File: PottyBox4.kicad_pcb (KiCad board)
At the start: 2 copper layers, 46 parts, among them IC1 ESP32-WROVER-B_(16MB), J1 Sensor 1, J10 Flush 2, J2 Touch 1, J3 24VAC, J4 Sensor 2, J5 Touch 2, J6 Qwiic, J7 DEGUG, J8 Exhaust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

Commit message: Finish up schematic, start layout work
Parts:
- added D10: PWR, LED_SMD:LED_0603_1608Metric_Pad1.05x0.95mm_HandSolder, F.Cu at (176.1, 95.3)
- added D9: STATUS, ASMB-KTF0-0A306:ASMBKTF00A306, F.Cu at (118.5, 124.5)
- added R16: 1k, Resistor_SMD:R_0603_1608Metric_Pad1.05x0.95mm_HandSolder, F.Cu at (117.5, 121.0)
- added R17: 1k, Resistor_SMD:R_0603_1608Metric_Pad1.05x0.95mm_HandSolder, F.Cu at (171.6, 107.5)
- added SW1: BOOT, PTS526_SMG15_SMTR2_LFS:PTS526SMG15SMTR2LFS, F.Cu at (227.1, 125.7)
- added SW2: RESET, PTS526_SMG15_SMTR2_LFS:PTS526SMG15SMTR2LFS, F.Cu at (227.1, 117.6)
- D2: value GREEN -> S1
- D3: value GREEN -> S2
- D4: value F1 -> S1S
- D5: value F2 -> S2S
- D6: value EX -> F1
- D7: value STATUS -> F2; footprint ASMB-KTF0-0A306:ASMBKTF00A306 -> LED_SMD:LED_0603_1608Metric_Pad1.05x0.95mm_HandSolder
- D8: value PWR -> EX
- IC1: value ESP32-WROVER-B_(16MB) -> ESP32-WROVER-B
- J3: value 24VAC -> Sensor 2; footprint SparkFun-Connectors:SCREWTERMINAL-3.5MM-2 -> Connector_JST:JST_SH_SM06B-SRSS-TB_1x06-1MP_P1.00mm_Horizontal
- J4: value Sensor 2 -> Touch 2; footprint Connector_JST:JST_SH_SM06B-SRSS-TB_1x06-1MP_P1.00mm_Horizontal -> Connector_JST:JST_PH_S2B-PH-K_1x02_P2.00mm_Horizontal
- J5: value Touch 2 -> Qwiic; footprint Connector_JST:JST_PH_S2B-PH-K_1x02_P2.00mm_Horizontal -> Connector_JST:JST_SH_SM04B-SRSS-TB_1x04-1MP_P1.00mm_Horizontal
- J6: value Qwiic -> 24VAC; footprint Connector_JST:JST_SH_SM04B-SRSS-TB_1x04-1MP_P1.00mm_Horizontal -> SparkFun-Connectors:SCREWTERMINAL-3.5MM-2
- K1, K2: value G3VM-61VY3(TR05) -> G3VM-61VY3
- R1, R2, R5: value 10k -> 1k
- R11, R12: value 1k -> 220
- R3, R4, R7: value 1k -> 10k
- R8, R9: value 220 -> 1k
- U1: value RPM3.3-2.0 -> OKI-78SR-3.3/1.5-W36H-C; footprint Converter_DCDC:Converter_DCDC_RECOM_RPMx.x-x.0 -> Converter_DCDC:Converter_DCDC_muRata_OKI-78SR_Horizontal
- moved J9 211.8 mm to (34.2, 115.8)
- moved R8 211.0 mm to (33.2, 103.5), turned to 90 degrees
- moved R10 199.1 mm to (37.8, 102.5), turned to 180 degrees
- moved C1 196.3 mm to (44.8, 50.2), turned to 90 degrees
- moved R11 193.7 mm to (50.2, 102.5), turned to 180 degrees
- moved K1 192.1 mm to (37.2, 107.8), turned to -90 degrees
- moved R12 191.1 mm to (72.8, 106.8), turned to 180 degrees
- moved R9 190.3 mm to (45.8, 103.5), turned to 90 degrees
- moved J10 186.5 mm to (46.8, 115.8)
- moved K3 176.2 mm to (78.2, 118.2), turned to 90 degrees
- moved R13 173.6 mm to (69.2, 106.8)
- moved U1 173.1 mm to (44.8, 60.8)
- moved K2 173.1 mm to (49.8, 107.8), turned to -90 degrees
- moved D8 172.4 mm to (65.8, 106.8)
- moved J6 160.3 mm to (50.5, 49.0)
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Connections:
- IC1 pad 10: (no net) -> /FLUSH1
- IC1 pad 11: (no net) -> /FLUSH2
- IC1 pad 12: (no net) -> /LED_SR
- IC1 pad 13: (no net) -> /LED_SG
- IC1 pad 14: (no net) -> /LED_SB
- IC1 pad 16: (no net) -> /EXHAUST
- IC1 pad 24: (no net) -> /SHUT1
- IC1 pad 26: (no net) -> /SHUT2
- IC1 pad 29: (no net) -> /INT1
- IC1 pad 30: (no net) -> /INT2
- IC1 pad 31: (no net) -> /LED_S1
- IC1 pad 37: (no net) -> /LED_S2
- J1 pad 5: (no net) -> /INT1
- J1 pad 6: (no net) -> /SHUT1
- J3 pad 1: /24VAC1 -> GND
- J3 pad 2: /24VAC2 -> +3V3
- J4 pad 2: +3V3 -> /TOUCH2
- J5 pad 2: /TOUCH2 -> +3V3
- J6 pad 1: GND -> /24VAC1
- J6 pad 2: +3V3 -> /24VAC2
- R1 pad 1: Net-(Q1-Pad1) -> Net-(D2-Pad2)
- R1 pad 2: /DTR -> /LED_S1
- R10 pad 1: Net-(K3-Pad3) -> Net-(K1-Pad1)
- R10 pad 2: (no net) -> /FLUSH1
- R11 pad 1: Net-(D6-Pad2) -> Net-(K2-Pad1)
- R11 pad 2: (no net) -> /FLUSH2
- R12 pad 1: Net-(D7-Pad2) -> Net-(K3-Pad3)
- R12 pad 2: (no net) -> /EXHAUST
- R13 pad 1: Net-(D7-Pad4) -> Net-(D8-Pad2)
- R13 pad 2: (no net) -> /EXHAUST
- R14 pad 1: Net-(D7-Pad3) -> Net-(D9-Pad2)
- R14 pad 2: (no net) -> /LED_SR
- R15 pad 1: Net-(D8-Pad2) -> Net-(D9-Pad4)
- R15 pad 2: +3V3 -> /LED_SB
- R2 pad 1: Net-(Q2-Pad1) -> Net-(D3-Pad2)
- R2 pad 2: /RTS -> /LED_S2
- R3 pad 1: Net-(D2-Pad2) -> Net-(Q1-Pad1)
- R3 pad 2: (no net) -> /DTR
- R4 pad 1: Net-(D3-Pad2) -> Net-(Q2-Pad1)
- R4 pad 2: (no net) -> /RTS
- R5 pad 1: +3V3 -> Net-(D4-Pad2)
- R5 pad 2: /EN -> /SHUT1
- R6 pad 1: Net-(D4-Pad2) -> Net-(D5-Pad2)
- R6 pad 2: (no net) -> /SHUT2
- R7 pad 1: Net-(D5-Pad2) -> +3V3
- R7 pad 2: (no net) -> /EN
- R8 pad 1: Net-(K1-Pad1) -> Net-(D6-Pad2)
- R8 pad 2: (no net) -> /FLUSH1
- R9 pad 1: Net-(K2-Pad1) -> Net-(D7-Pad2)
- R9 pad 2: (no net) -> /FLUSH2
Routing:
- net /RTS: track 0.00 -> 21.8 mm, vias 0 -> 1
- net /EN: track 0.00 -> 11.6 mm
- net /DTR: track 0.00 -> 9.91 mm
- net /IO0: track 0.00 -> 9.43 mm
- net Net-(D9-Pad4): track 0.00 -> 4.50 mm
- net Net-(Q1-Pad1): track 0.00 -> 3.99 mm
- net Net-(D9-Pad3): track 0.00 -> 2.07 mm
- net Net-(D9-Pad2): track 0.00 -> 2.07 mm
- net Net-(Q2-Pad1): track 0.00 -> 1.99 mm

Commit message: Wire up sensor ports, LEDs, and Qwiic port to ESP32
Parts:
- moved J1 100.2 mm to (122.5, 181.5), turned to 90 degrees
- moved R5 98.4 mm to (117.2, 176.8)
- moved D2 98.1 mm to (117.2, 181.5)
- moved D4 91.1 mm to (117.2, 178.5), turned to 180 degrees
- moved R1 90.8 mm to (117.2, 183.2), turned to 180 degrees
- moved R6 84.3 mm to (117.2, 166.8)
- moved J7 82.7 mm to (121.5, 188.5), turned to 90 degrees
- moved IC1 78.9 mm to (104.0, 172.5)
- moved J3 71.6 mm to (122.5, 171.5), turned to 90 degrees
- moved D3 68.6 mm to (117.2, 171.5)
- moved R2 68.1 mm to (117.2, 173.2), turned to 180 degrees
- moved J5 56.3 mm to (122.5, 162.5), turned to 90 degrees
- moved D5 54.7 mm to (117.2, 168.5), turned to 180 degrees
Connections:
- IC1 pad 24: /SHUT1 -> /LED_S1
- IC1 pad 26: /SHUT2 -> /INT1
- IC1 pad 29: /INT1 -> /SHUT1
- IC1 pad 30: /INT2 -> /LED_S2
- IC1 pad 31: /LED_S1 -> /INT2
- IC1 pad 37: /LED_S2 -> /SHUT2
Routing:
- net /SDA: track 0.00 -> 38.1 mm, vias 0 -> 2
- net /SCL: track 0.00 -> 35.9 mm, vias 0 -> 4
- net Net-(J8-Pad1): track 0.00 -> 13.3 mm
- net Net-(C1-Pad1): track 0.00 -> 10.6 mm
- net /IO15: track 0.00 -> 10.5 mm
- net /SHUT2: track 0.00 -> 8.80 mm
- net /SHUT1: track 0.00 -> 8.73 mm
- net /INT1: track 0.00 -> 7.57 mm
- net Net-(J8-Pad2): track 0.00 -> 7.31 mm
- net /24VAC2: track 0.00 -> 7.13 mm
- net /24VAC1: track 0.00 -> 7.13 mm
- net Net-(J9-Pad2): track 0.00 -> 5.07 mm
- net Net-(J10-Pad2): track 0.00 -> 5.07 mm
- net Net-(K3-Pad3): track 0.00 -> 4.65 mm
- net /LED_S1: track 0.00 -> 3.73 mm
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
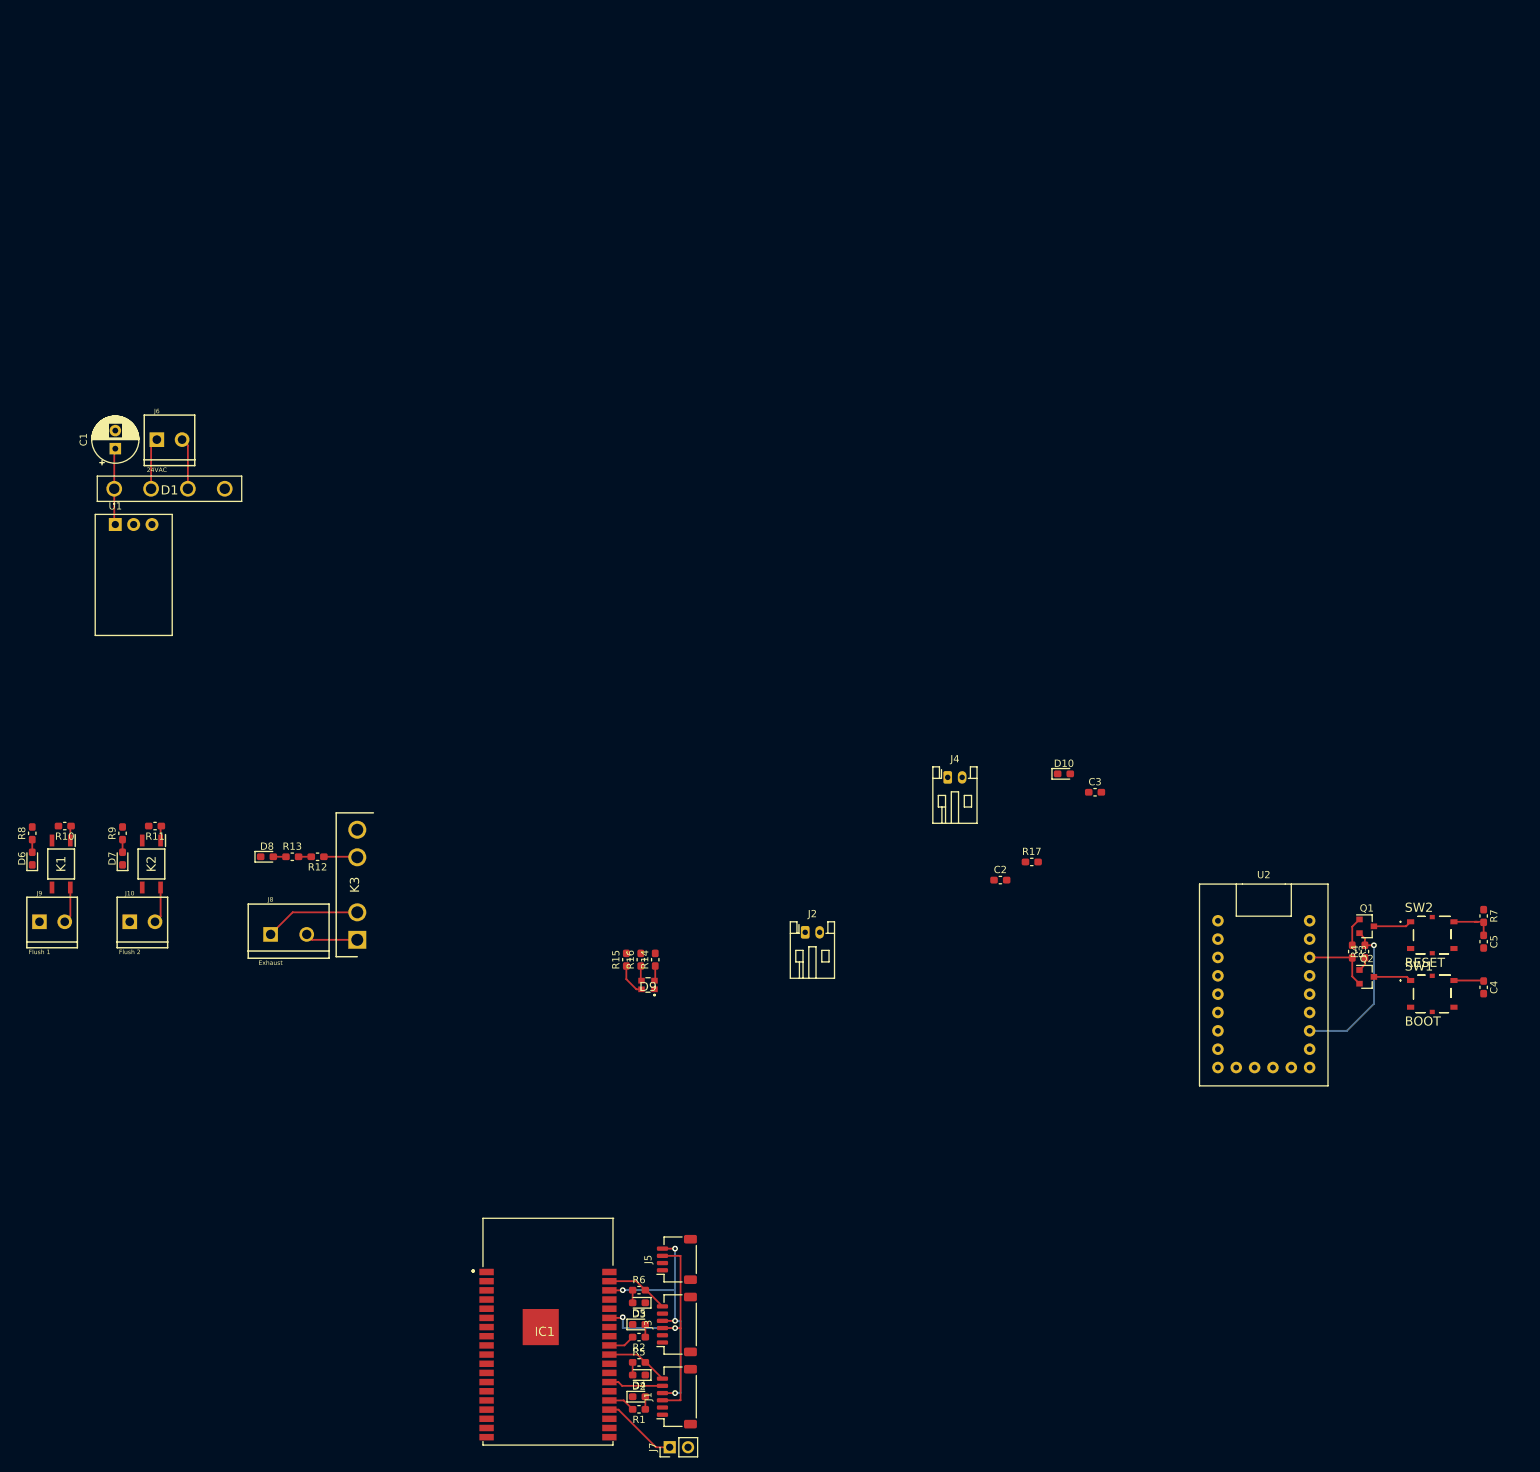
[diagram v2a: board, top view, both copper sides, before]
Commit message: ERC/DRC down to a minimum
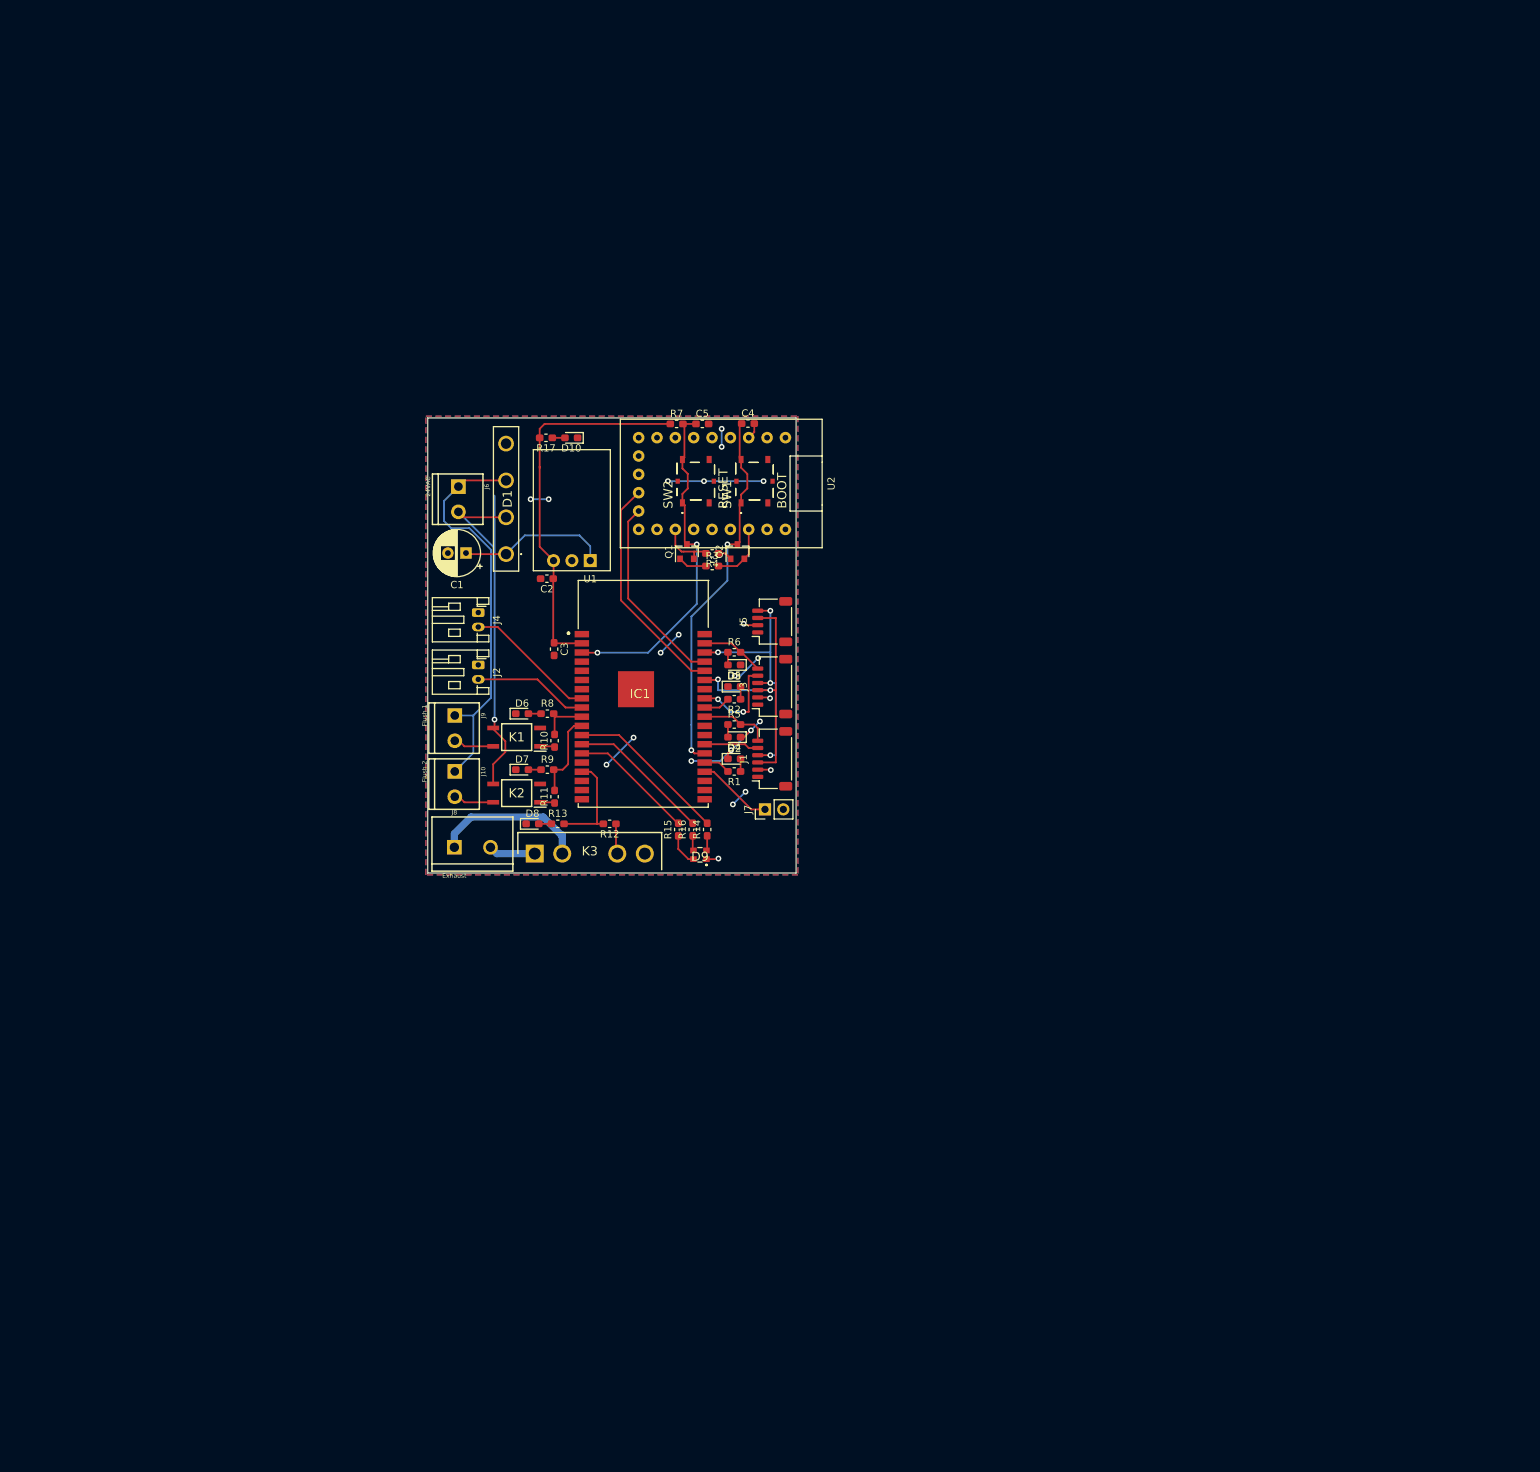
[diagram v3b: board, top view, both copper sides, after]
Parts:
- moved R7 130.9 mm to (122.5, 46.8), turned to 0 degrees
- moved C5 129.8 mm to (126.0, 46.8), turned to 0 degrees
- moved C4 128.3 mm to (132.3, 46.8), turned to 0 degrees
- moved SW2 119.8 mm to (125.1, 54.8), turned to 90 degrees
- moved SW1 117.7 mm to (133.2, 54.8), turned to 90 degrees
- moved Q1 107.5 mm to (123.9, 64.5), turned to 90 degrees
- moved R4 105.9 mm to (127.4, 64.8), turned to 180 degrees
- moved Q2 105.1 mm to (130.9, 64.5), turned to 90 degrees
- moved R3 103.4 mm to (127.4, 66.5), turned to 0 degrees
- moved U2 102.3 mm to (128.6, 55.1), turned to -90 degrees
- moved D2 89.3 mm to (130.4, 93.2)
- moved D3 89.3 mm to (130.4, 83.2)
- moved D4 89.3 mm to (130.4, 90.2)
- moved D5 89.3 mm to (130.4, 80.2)
- moved IC1 89.3 mm to (117.2, 84.2)
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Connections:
- J6 pad 1: /24VAC1 -> /24VAC2
- J6 pad 2: /24VAC2 -> /24VAC1
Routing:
- net +3V3: track 0.00 -> 60.2 mm, vias 0 -> 4
- net GND: track 0.00 -> 51.1 mm, vias 0 -> 19
- net /24VAC2: track 7.13 -> 56.2 mm
- net /24VAC1: track 7.13 -> 55.6 mm, vias 0 -> 1
- net /IO0: track 9.43 -> 51.8 mm, vias 0 -> 2
- net /EN: track 11.6 -> 48.0 mm, vias 0 -> 2
- net /RXD0: track 0.00 -> 31.6 mm
- net /TXD0: track 0.00 -> 26.9 mm
- net /LED_SR: track 0.00 -> 22.4 mm
- net /LED_SG: track 0.00 -> 19.9 mm
- net /TOUCH2: track 0.00 -> 18.0 mm
- net /LED_SB: track 0.00 -> 17.4 mm
- net /TOUCH1: track 0.00 -> 15.5 mm
- net /RTS: track 21.8 -> 7.93 mm, vias 1 -> 0
- net /INT2: track 0.00 -> 13.1 mm, vias 0 -> 2
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- added copper zone on B.Cu, net +3V3
- added copper zone on F.Cu, net GND
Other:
- board outline added: 51 x 63 mm

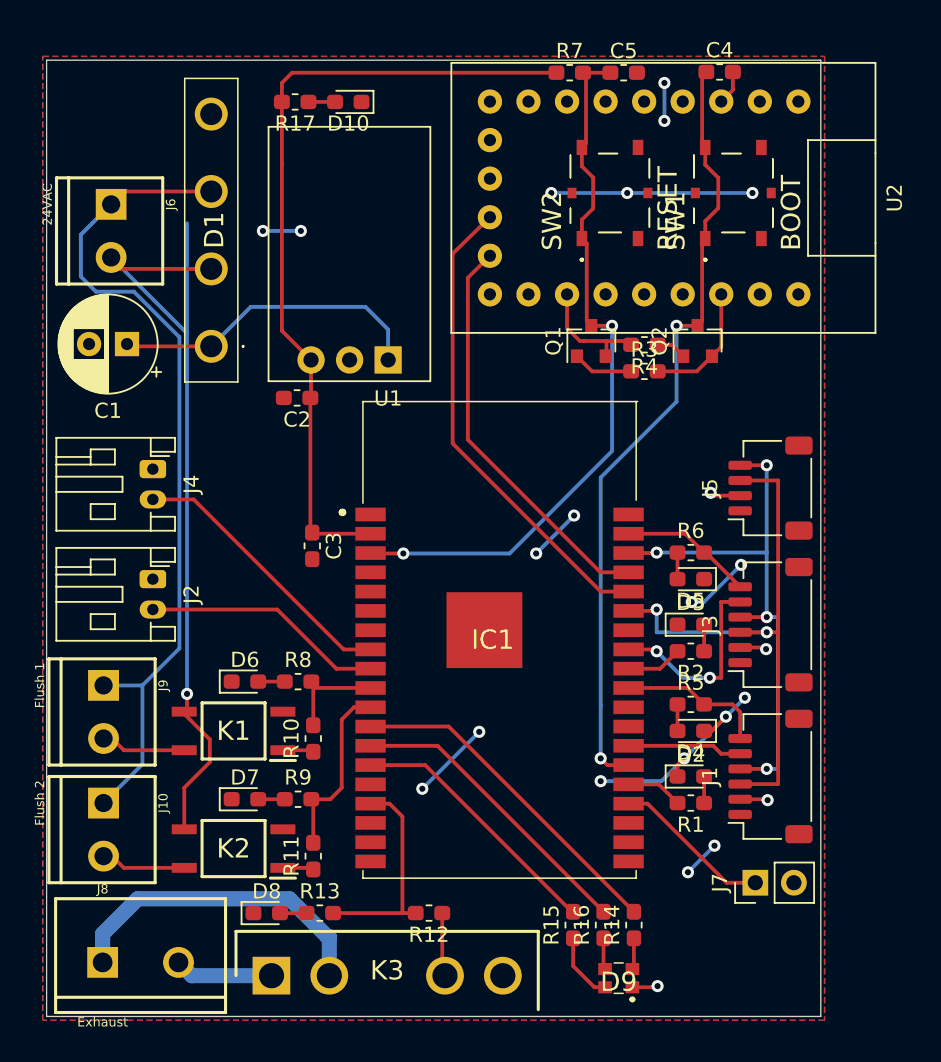
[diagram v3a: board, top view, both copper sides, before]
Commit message: Layout complete, clean ERC/DRC
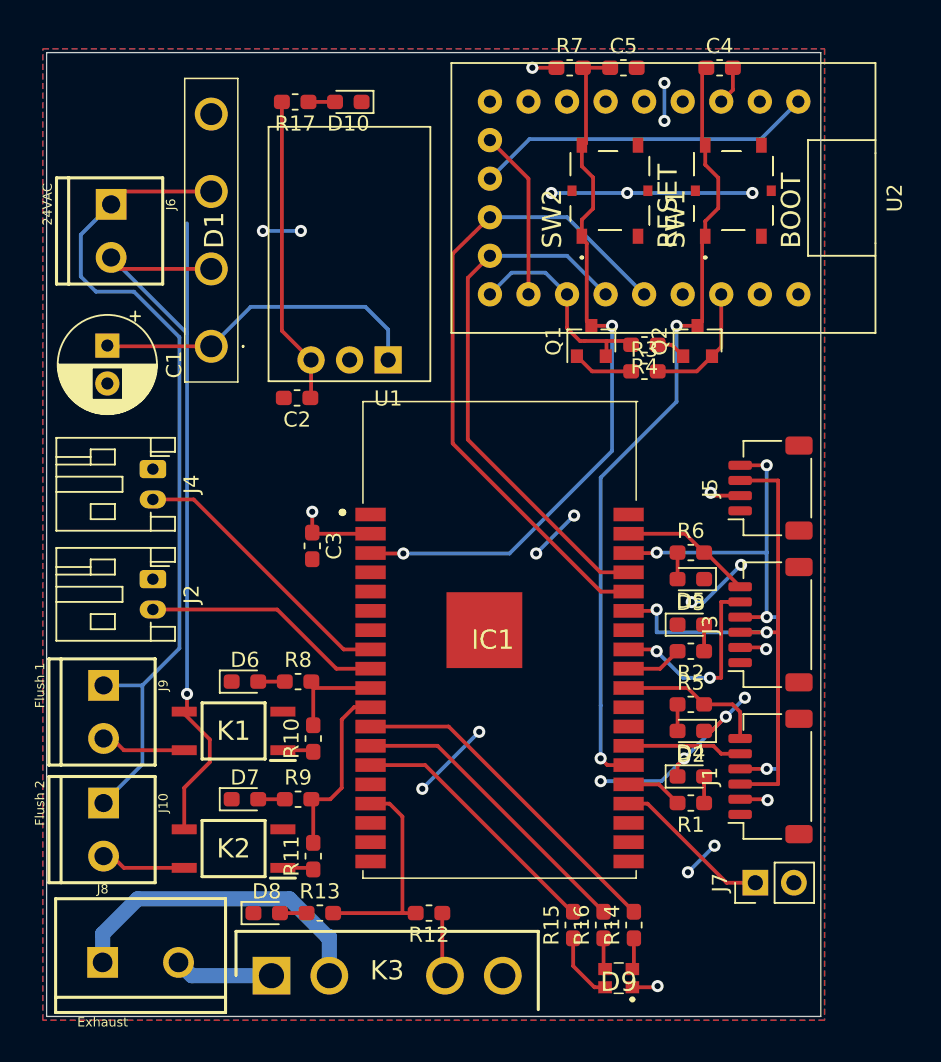
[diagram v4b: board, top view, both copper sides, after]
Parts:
- moved C1 1.30 mm to (92.0, 64.8), turned to -90 degrees
- moved C5 0.33 mm to (126.0, 46.5)
- moved R7 0.33 mm to (122.5, 46.5)
- moved C4 0.28 mm to (132.3, 46.5)
- moved SW1 0.15 mm to (133.2, 54.6)
- moved SW2 0.15 mm to (125.1, 54.6)
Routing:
- net +3V3: track 60.2 -> 34.4 mm, vias 4 -> 6
- net Net-(U2-Pad1): track 0.00 -> 22.4 mm
- net /RXD0: track 31.6 -> 43.8 mm
- net Net-(U2-Pad9): track 0.00 -> 11.2 mm
- net /TXD0: track 26.9 -> 35.6 mm
- net /RTS: track 7.93 -> 14.2 mm
- net Net-(C1-Pad1): track 21.2 -> 22.4 mm
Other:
- board size 51 x 63 mm -> 51 x 63.5 mm
